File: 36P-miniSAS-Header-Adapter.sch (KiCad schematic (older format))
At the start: 2 parts, among them J1 1888863-4, J2 Conn_02x18

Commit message: Add layout drawing
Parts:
- added H1, H2: MountingHole, MountingHole:MountingHole_3.2mm_M3, symbol Mechanical:MountingHole
- J1: footprint TE_1888863-4 -> footprints:TE_1888863-4
- J2: footprint (none) -> Connector_PinHeader_2.54mm:PinHeader_2x18_P2.54mm_Vertical
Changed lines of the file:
@@
 $EndDescr
-$Comp
-L Connector_Generic:Conn_02x18_Odd_Even J2
-U 1 1 60AA8480
-P 7300 3700
-F 0 "J2" H 7350 4717 50  0000 C CNN
-F 1 "Conn_02x18" H 7350 4626 50  0000 C CNN
-F 2 "" H 7300 3700 50  0001 C CNN
-F 3 "~" H 7300 3700 50  0001 C CNN
-	1    7300 3700
-	-1   0    0    -1
-$EndComp
 $Comp
 L 1888863-4:1888863-4 J1
@@
 F 0 "J1" H 4200 5167 50  0000 C CNN
 F 1 "1888863-4" H 4200 5076 50  0000 C CNN
-F 2 "TE_1888863-4" H 4200 3900 50  0001 L BNN
+F 2 "footprints:TE_1888863-4" H 4200 3900 50  0001 L BNN
 F 3 "1888863-4" H 4200 3900 50  0001 L BNN
 F 4 "Compliant" H 4200 3900 50  0001 L BNN "Field4"
@@
 	3700 4600 2650 4600
 $Comp
-L power:GND #PWR?
+L power:GND #PWR0101
 U 1 1 60AC75AD
 P 3050 5000
-F 0 "#PWR?" H 3050 4750 50  0001 C CNN
+F 0 "#PWR0101" H 3050 4750 50  0001 C CNN
 F 1 "GND" H 3055 4827 50  0000 C CNN
 F 2 "" H 3050 5000 50  0001 C CNN
@@
 Wire Wire Line
 	3050 4800 3050 5000
-Wire Wire Line
-	7500 2900 8300 2900
-Wire Wire Line
-	7500 3000 8300 3000
-Wire Wire Line
-	7500 3100 8300 3100
-Wire Wire Line
-	7500 3200 8300 3200
-Wire Wire Line
-	7500 3300 8300 3300
-Wire Wire Line
-	7500 3400 8300 3400
-Wire Wire Line
-	7500 3500 8300 3500
-Wire Wire Line
-	7500 3600 8300 3600
-Wire Wire Line
-	7500 3700 8300 3700
-Wire Wire Line
-	7500 3800 8300 3800
-Wire Wire Line
-	7500 3900 8300 3900
-Wire Wire Line
-	7500 4000 8300 4000
-Wire Wire Line
-	7500 4100 8300 4100
-Wire Wire Line
-	7500 4200 8300 4200
-Wire Wire Line
-	7500 4300 8300 4300
-Wire Wire Line
-	7500 4400 8300 4400
-Wire Wire Line
-	7500 4500 8300 4500
-Wire Wire Line
-	7500 4600 8300 4600
-Wire Wire Line
-	4700 2900 7000 2900
-Wire Wire Line
-	4700 3000 7000 3000
-Wire Wire Line
-	4700 3100 7000 3100
-Wire Wire Line
-	4700 3200 7000 3200
-Wire Wire Line
-	4700 3300 7000 3300
-Wire Wire Line
-	4700 3400 7000 3400
-Wire Wire Line
-	4700 3500 7000 3500
-Wire Wire Line
-	4700 3600 7000 3600
-Wire Wire Line
-	4700 3700 7000 3700
-Wire Wire Line
-	4700 3800 7000 3800
-Wire Wire Line
-	4700 3900 7000 3900
-Wire Wire Line
-	4700 4000 7000 4000
-Wire Wire Line
-	4700 4100 7000 4100
-Wire Wire Line
-	4700 4200 7000 4200
-Wire Wire Line
-	4700 4300 7000 4300
-Wire Wire Line
-	4700 4400 7000 4400
-Wire Wire Line
-	4700 4500 7000 4500
-Wire Wire Line
-	4700 4600 7000 4600
 Text Label 2950 2900 0    50   ~ 0
 A1
@@
 Text Label 7900 4600 0    50   ~ 0
 A18
+Wire Wire Line
+	4700 4600 7000 4600
+Wire Wire Line
+	4700 4500 7000 4500
+Wire Wire Line
+	4700 4400 7000 4400
+Wire Wire Line
+	4700 4300 7000 4300
+Wire Wire Line
+	4700 4200 7000 4200
+Wire Wire Line
+	4700 4100 7000 4100
+Wire Wire Line
+	4700 4000 7000 4000
+Wire Wire Line
+	4700 3900 7000 3900
+Wire Wire Line
+	4700 3800 7000 3800
+Wire Wire Line
+	4700 3700 7000 3700
+Wire Wire Line
+	4700 3600 7000 3600
+Wire Wire Line
+	4700 3500 7000 3500
+Wire Wire Line
+	4700 3400 7000 3400
+Wire Wire Line
+	4700 3300 7000 3300
+Wire Wire Line
+	4700 3200 7000 3200
+Wire Wire Line
+	4700 3100 7000 3100
+Wire Wire Line
+	4700 3000 7000 3000
+Wire Wire Line
+	4700 2900 7000 2900
+Wire Wire Line
+	7500 4600 8300 4600
+Wire Wire Line
+	7500 4500 8300 4500
+Wire Wire Line
+	7500 4400 8300 4400
+Wire Wire Line
+	7500 4300 8300 4300
+Wire Wire Line
+	7500 4200 8300 4200
+Wire Wire Line
+	7500 4100 8300 4100
+Wire Wire Line
+	7500 4000 8300 4000
+Wire Wire Line
+	7500 3900 8300 3900
+Wire Wire Line
+	7500 3800 8300 3800
+Wire Wire Line
+	7500 3700 8300 3700
+Wire Wire Line
+	7500 3600 8300 3600
+Wire Wire Line
+	7500 3500 8300 3500
+Wire Wire Line
+	7500 3400 8300 3400
+Wire Wire Line
+	7500 3300 8300 3300
+Wire Wire Line
+	7500 3200 8300 3200
+Wire Wire Line
+	7500 3100 8300 3100
+Wire Wire Line
+	7500 3000 8300 3000
+Wire Wire Line
+	7500 2900 8300 2900
+$Comp
+L Connector_Generic:Conn_02x18_Odd_Even J2
+U 1 1 60AA8480
+P 7300 3700
+F 0 "J2" H 7350 4717 50  0000 C CNN
+F 1 "Conn_02x18" H 7350 4626 50  0000 C CNN
+F 2 "Connector_PinHeader_2.54mm:PinHeader_2x18_P2.54mm_Vertical" H 7300 3700 50  0001 C CNN
+F 3 "~" H 7300 3700 50  0001 C CNN
+	1    7300 3700
+	-1   0    0    -1
+$EndComp
+$Comp
+L Mechanical:MountingHole H1
+U 1 1 60AE2E30
+P 4500 5500
+F 0 "H1" H 4600 5546 50  0000 L CNN
+F 1 "MountingHole" H 4600 5455 50  0000 L CNN
+F 2 "MountingHole:MountingHole_3.2mm_M3" H 4500 5500 50  0001 C CNN
+F 3 "~" H 4500 5500 50  0001 C CNN
+	1    4500 5500
+	1    0    0    -1
+$EndComp
+$Comp
+L Mechanical:MountingHole H2
+U 1 1 60AE35B5
+P 5500 5500
+F 0 "H2" H 5600 5546 50  0000 L CNN
+F 1 "MountingHole" H 5600 5455 50  0000 L CNN
+F 2 "MountingHole:MountingHole_3.2mm_M3" H 5500 5500 50  0001 C CNN
+F 3 "~" H 5500 5500 50  0001 C CNN
+	1    5500 5500
+	1    0    0    -1
+$EndComp
 $EndSCHEMATC

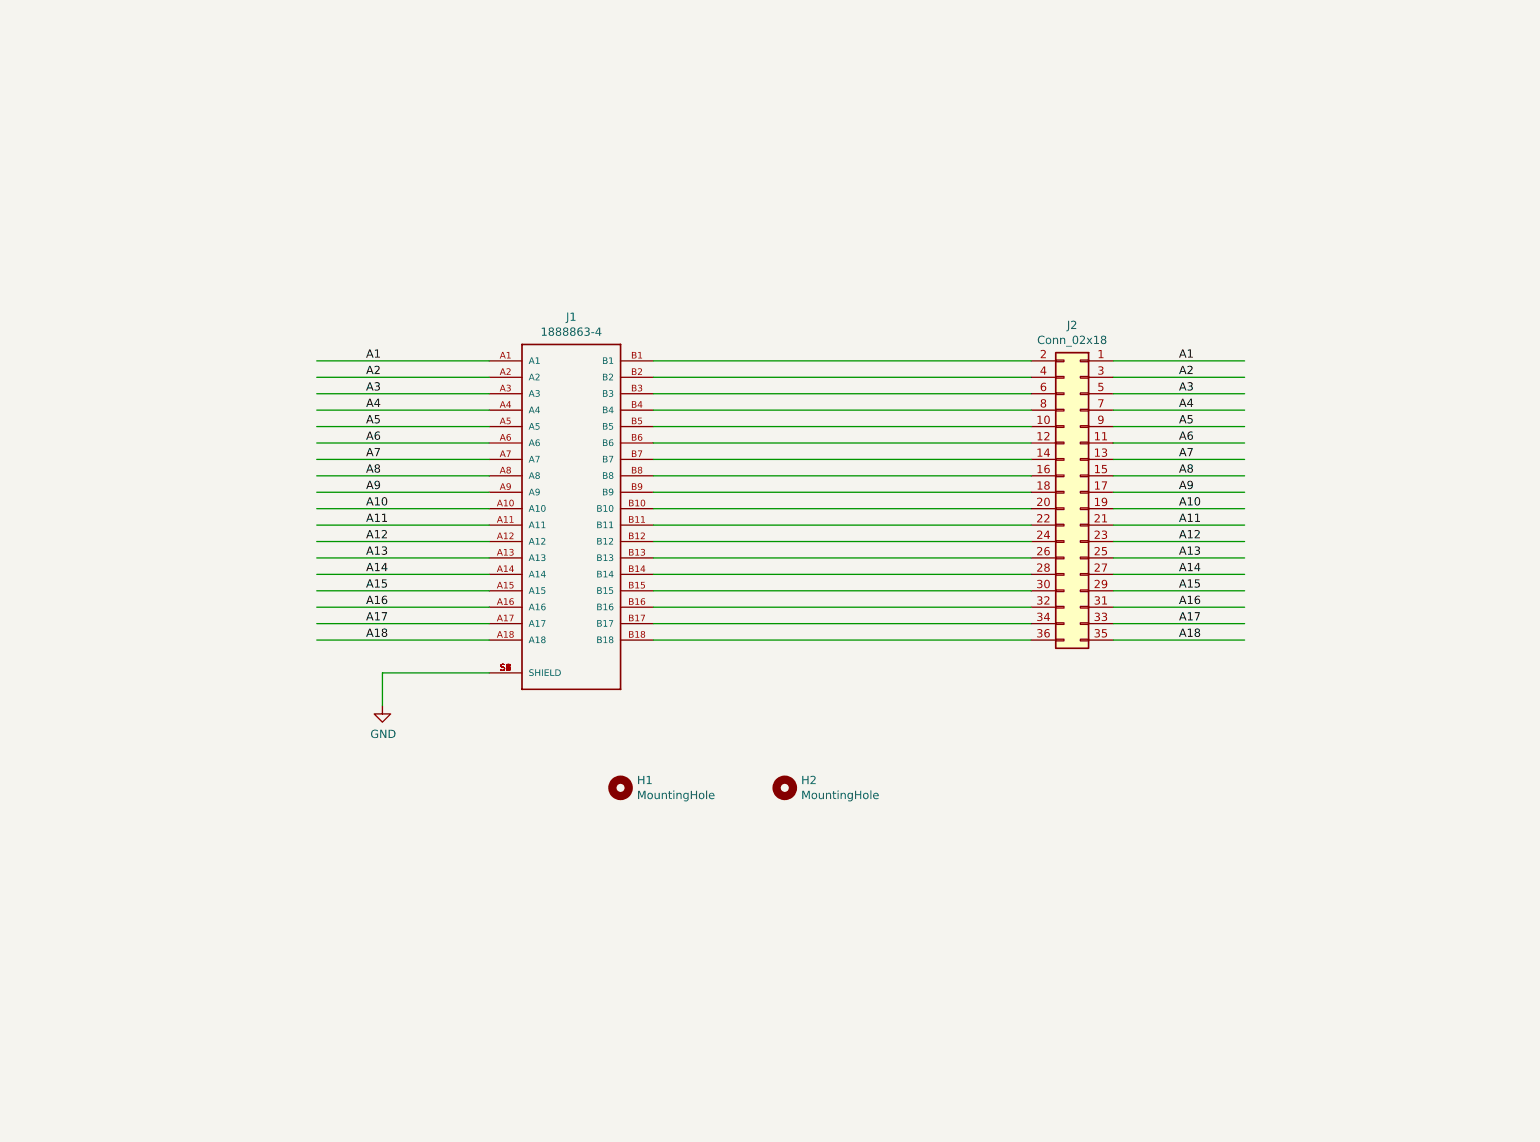
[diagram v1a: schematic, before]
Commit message: Finalize pcb routing
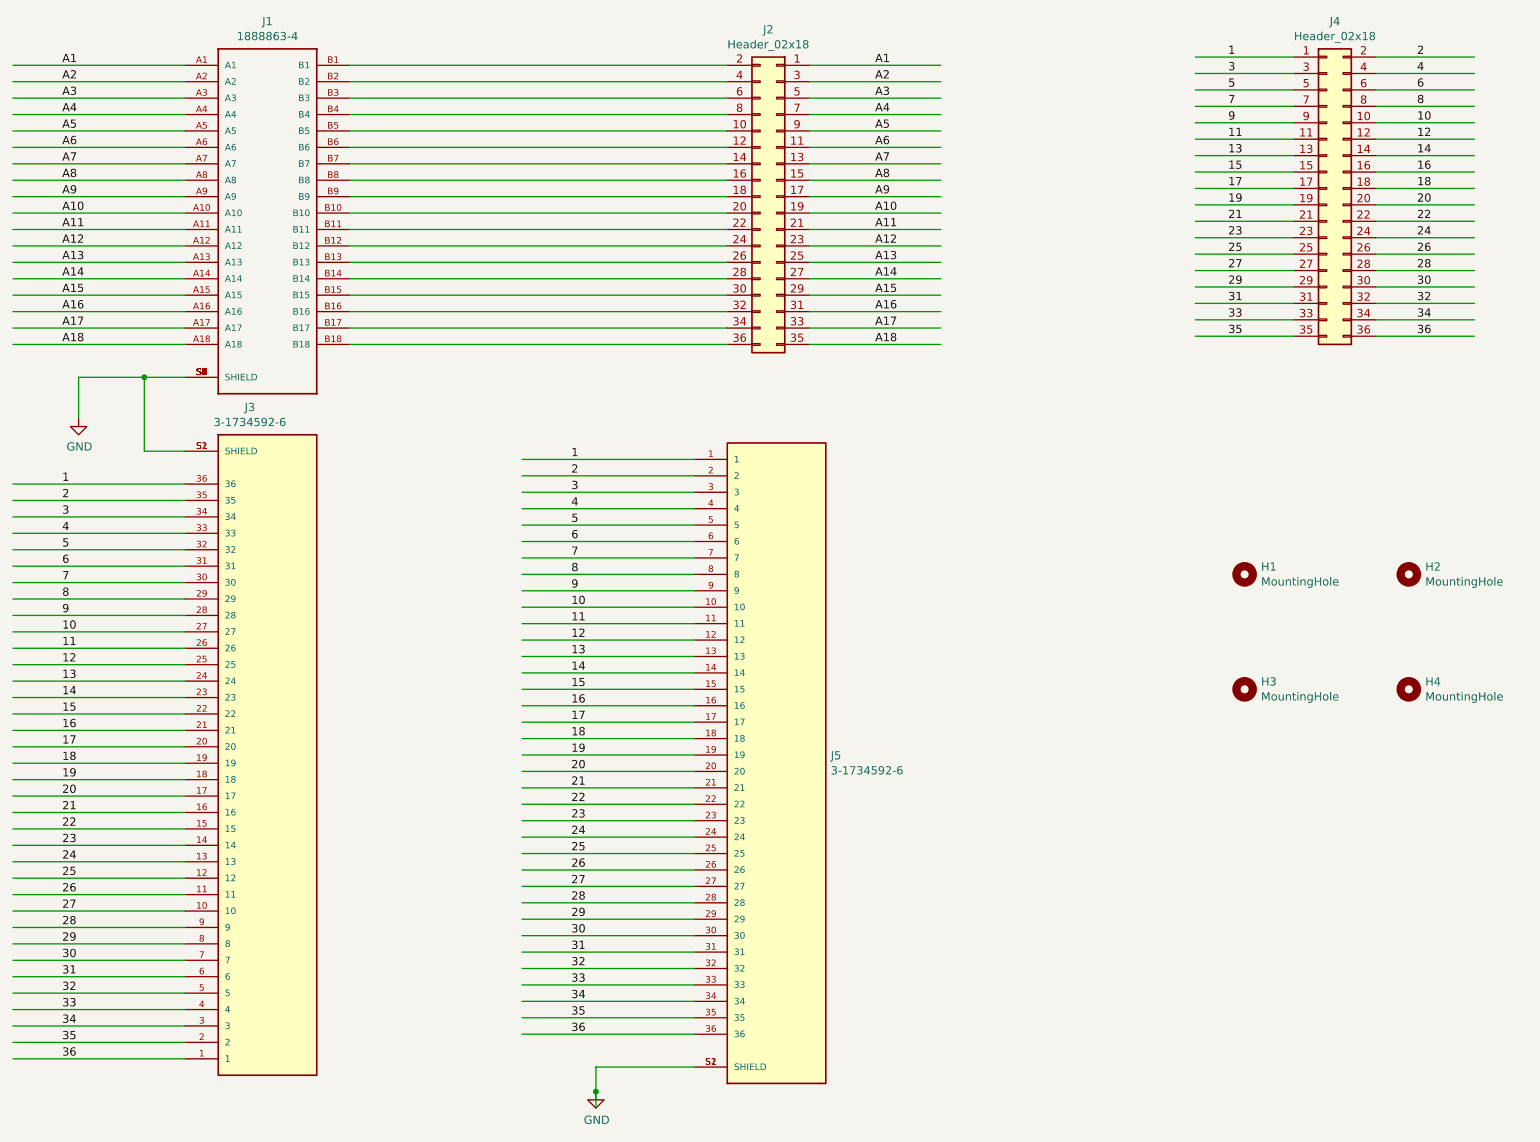
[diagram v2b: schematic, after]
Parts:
- added H3, H4: MountingHole, MountingHole:MountingHole_3.2mm_M3, symbol Mechanical:MountingHole
- added J3, J5: 3-1734592-6, footprints:TE_3-1734592-6, symbol TE_3-1734592-6:3-1734592-6
- added J4: Header_02x18, Connector_PinHeader_2.54mm:PinHeader_2x18_P2.54mm_Vertical, symbol Connector_Generic:Conn_02x18_Odd_Even
- J2: value Conn_02x18 -> Header_02x18
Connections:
- net labels added: 1, 10, 11, 12, 13, 14, 15, 16, 17, 18, 19, 2, 20, 21, 22, 23, 24, 25, 26, 27, 28, 29, 3, 30, 31, 32, 33, 34, 35, 36, 4, 5, 6, 7, 8, 9
- wire segments 56 -> 170
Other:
- moved on the sheet: H1, H2, J1, J2
